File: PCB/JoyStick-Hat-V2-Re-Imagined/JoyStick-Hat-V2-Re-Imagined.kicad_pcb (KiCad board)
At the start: 4 copper layers, 123 x 56 mm, 98 parts, among them J1 20021121-00010C4LF, J11 0705430002, J2 BU2032SM-JJ-GTR, J3 0901301210, J4 0901301108, J5 RJHSE-5381, J6 1757242, J7 SBH11-PBPC-D10-ST-BK, J8 0901301108, J9 0705430002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

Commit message: V2 PCB First PAss Complete
First pass of V2 PCB Completeded !
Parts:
- added C23: C0402C104K9PACTU, AVR-KiCAD-Lib-Resistors:R0402, F.Cu at (120.5, 85.2)
- added C24: GRM155R60J475ME47D, AVR-KiCAD-Lib-Capacitors:C0402, F.Cu at (119.5, 85.2)
- added C30: C0805C103KCRACAUTO, AVR-KiCAD-Lib-Capacitors:C0805, F.Cu at (107.2, 66.8)
- added D8: SMAJ30CA, AVR-KiCAD-Lib-Diodes:SMAJ30CA, F.Cu at (101.9, 64.6)
- added J10: 0901301210, AVR-KiCAD-Lib-Connectors:CON_901301212_MOL, F.Cu at (103.8, 97.0)
- added J12: DX07S016JA1R1500, AVR-KiCAD-Lib-Connectors:JAE_DX07S016JA1R1500, F.Cu at (105.0, 74.2)
- added L4: MI0603K300R-10, AVR-KiCAD-Lib-Inductors:MI0603K300R-10, F.Cu at (109.0, 70.0)
- added R11: RC0402FR-0710KL, AVR-KiCAD-Lib-Resistors:R0402, F.Cu at (110.8, 72.2)
- added R17: RC1206FR-071ML, AVR-KiCAD-Lib-Resistors:R1206, F.Cu at (104.9, 66.6)
- added R18: RC0402FR-0722RL, AVR-KiCAD-Lib-Resistors:R0402, F.Cu at (110.7, 73.3)
- added R22: RC0402FR-0722RL, AVR-KiCAD-Lib-Resistors:R0402, F.Cu at (110.7, 74.3)
- J1, R2, R3, R4, R6, R7: moved to B.Cu
- moved R2 15.4 mm to (120.0, 99.8)
- moved R3 12.9 mm to (120.0, 98.2)
- moved J1 10.8 mm to (114.5, 96.8)
- moved R4 10.6 mm to (120.0, 96.8)
- moved R6 8.84 mm to (120.0, 95.2)
- moved R7 7.85 mm to (120.0, 93.8)
- moved D3 7.52 mm to (154.1, 99.5)
- moved D4 7.52 mm to (154.1, 98.0)
- moved R12 7.52 mm to (151.1, 99.5)
- moved R13 7.52 mm to (151.1, 98.0)
- moved J7 6.30 mm to (129.4, 105.0)
- moved D7 6.02 mm to (154.1, 107.0)
- moved R16 6.02 mm to (151.1, 107.0)
- moved D1 3.05 mm to (154.1, 102.5)
- moved D2 3.05 mm to (154.1, 101.0)
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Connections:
- R12 pad 1: unconnected-(R12-Pad1) -> /STM32F446RET6-MCU/PE2
- R13 pad 1: unconnected-(R13-Pad1) -> /STM32F446RET6-MCU/PE3
- R14 pad 1: unconnected-(R14-Pad1) -> /STM32F446RET6-MCU/PB8
- R15 pad 1: unconnected-(R15-Pad1) -> /STM32F446RET6-MCU/PB9
- R16 pad 1: unconnected-(R16-Pad1) -> /STM32F446RET6-MCU/PB7
- U1 pad 1: unconnected-(U1-PE2-Pad1) -> /STM32F446RET6-MCU/PE2
- U1 pad 2: unconnected-(U1-PE3-Pad2) -> /STM32F446RET6-MCU/PE3
- U1 pad 52: unconnected-(U1-PB13-Pad52) -> Net-(U1-PB13)
- U1 pad 53: unconnected-(U1-PB14-Pad53) -> Net-(U1-PB14)
- U1 pad 54: unconnected-(U1-PB15-Pad54) -> Net-(U1-PB15)
- U1 pad 73: unconnected-(U1-VCAP_2-Pad73) -> Net-(U1-VCAP_2)
- U1 pad 93: unconnected-(U1-PB7-Pad93) -> /STM32F446RET6-MCU/PB7
- U1 pad 95: unconnected-(U1-PB8-Pad95) -> /STM32F446RET6-MCU/PB8
- U1 pad 96: unconnected-(U1-PB9-Pad96) -> /STM32F446RET6-MCU/PB9
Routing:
- net /STM32F446RET6-MCU/SWO_TDI: track 12.2 -> 49.1 mm, vias 1 -> 0
- net /STM32F446RET6-MCU/PC10: track 0.00 -> 35.6 mm, vias 0 -> 1
- net /STM32F446RET6-MCU/SWCLK_TCK: track 11.2 -> 46.6 mm, vias 1 -> 0
- net /STM32F446RET6-MCU/NRST: track 21.2 -> 55.0 mm
- net /STM32F446RET6-MCU/SWDIO_TMS: track 8.77 -> 40.9 mm
- net Net-(U1-PD7): track 0.00 -> 32.1 mm, vias 0 -> 2
- net /STM32F446RET6-MCU/NJTRST: track 15.0 -> 46.3 mm, vias 1 -> 0
- net /STM32F446RET6-MCU/PC11: track 0.00 -> 29.5 mm, vias 0 -> 1
- net /STM32F446RET6-MCU/PC12: track 1.17 -> 29.8 mm, vias 0 -> 1
- net /STM32F446RET6-MCU/PD3: track 2.00 -> 30.5 mm, vias 0 -> 1
- net /STM32F446RET6-MCU/PB7: track 0.00 -> 27.8 mm
- net /STM32F446RET6-MCU/PD5: track 2.41 -> 29.5 mm, vias 0 -> 1
- net /STM32F446RET6-MCU/PD1: track 1.58 -> 28.2 mm, vias 0 -> 1
- net /STM32F446RET6-MCU/PB8: track 0.00 -> 25.8 mm
- net /STM32F446RET6-MCU/PD6: track 2.62 -> 28.1 mm, vias 0 -> 1
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- added copper zone on B.Cu, net Net-(C30-Pad1)
- added copper zone on F.Cu, net Net-(C30-Pad1)
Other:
- board text added: "3v3"
- board text added: "DBDI"
- board text added: "DBRQ"
- board text added: "HEARTBEAT"
- board text added: "JTAG"
- board text added: "NJRT"
- board text added: "NRST"
- board text added: "PD10"
- board text added: "PD11"
- board text added: "PD12"
- board text added: "PD13"
- board text added: "PD8"
- board text added: "STM32 EXP"
- board text added: "TCK"
- board text added: "TDI"
- board text added: "TDO"
- board text added: "TMS"
- board text added: "USB 2.0"
- board text added: "VBAT"
- board text removed: "GND / PD13"
- board text removed: "GND / PD8"
- board text removed: "PD10 / PD9"
- board text removed: "PD12 / PD11"
- board text removed: "ST HEARTBEAT"

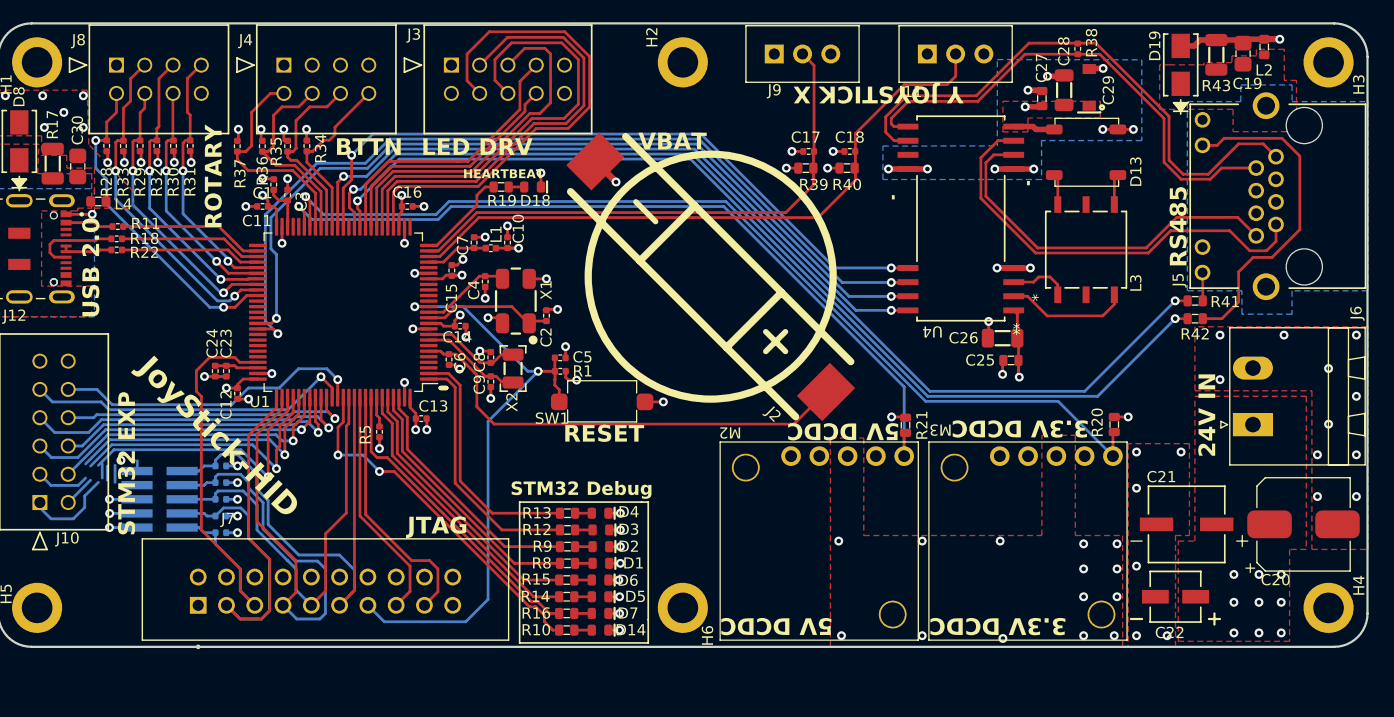
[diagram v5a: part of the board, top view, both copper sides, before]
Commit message: V2 Tweaks
More Tweaks to the completed V2 design. 3D renders of V2 design produced and added to img folder for documentation update coming in the next commit. Photos of prototype also added to img folder for documentation.
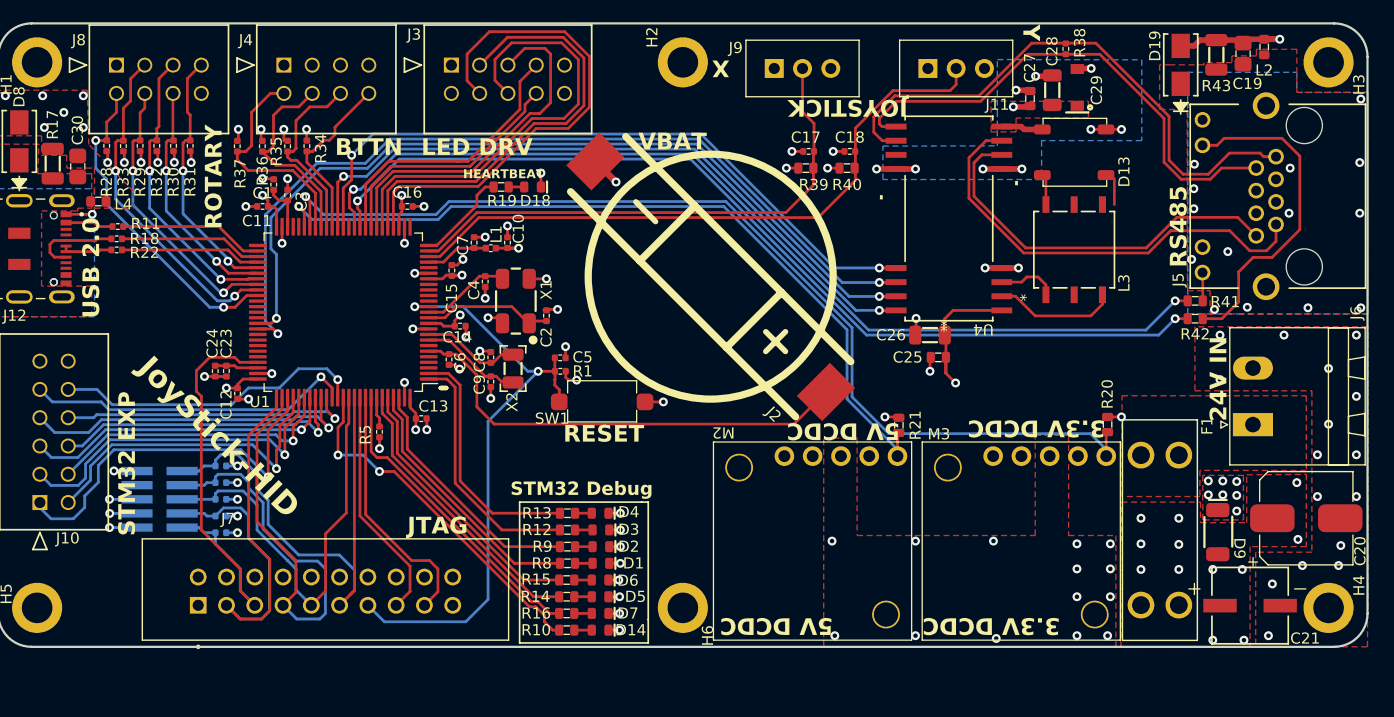
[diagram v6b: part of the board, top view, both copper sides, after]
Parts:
- removed C22: UUQ1H010MCL1GB, AVR-KiCAD-Lib-Capacitors:CAP_UUQ_4X5P4_NCH
- added D9: SMAJ24A, AVR-KiCAD-Lib-Diodes:SMAJ, F.Cu at (209.6, 99.7)
- added F1: 3557-2, AVR-KiCAD-Lib-Fuse-Holders:FUSE_3557-2, F.Cu at (204.3, 99.5)
- moved C21 9.26 mm to (212.4, 106.3), turned to 0 degrees
- moved C25 6.53 mm to (184.4, 84.0)
- moved C26 6.53 mm to (183.7, 82.0)
- moved J11 1.30 mm to (183.5, 58.0)
- moved J9 1.30 mm to (169.7, 58.0)
- moved C27 1.07 mm to (192.7, 60.8)
- moved C28 1.07 mm to (194.7, 60.0)
- moved C29 1.07 mm to (196.9, 59.8)
- moved D13 1.07 mm to (196.6, 65.6)
- moved L3 1.07 mm to (196.6, 74.3)
- moved R38 1.07 mm to (195.9, 56.3)
- moved U4 1.07 mm to (185.4, 71.5)
- moved C20 0.60 mm to (217.5, 98.5)
- moved M2 0.60 mm to (180.8, 92.9)
- moved M3 0.60 mm to (199.5, 92.9)
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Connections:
- J6 pad 1: +24V -> Net-(F1-Pad2)
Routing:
- net +3.3V: track 55.3 -> 60.7 mm
- net /RS485 To Motor Controller Interface/RS485_RX_LED: track 90.3 -> 85.7 mm
- net /RS485 To Motor Controller Interface/RS485_TX_LED: track 92.1 -> 87.6 mm
- net /Power/3.3V_PG: track 88.0 -> 91.6 mm
- net /STM32F446RET6-MCU/PC12: track 29.8 -> 31.1 mm
- net /STM32F446RET6-MCU/PC10: track 35.6 -> 34.3 mm
- net GND: track 70.8 -> 72.0 mm, vias 71 -> 77
- net /RS485 To Motor Controller Interface/Y_RS485: track 39.2 -> 40.3 mm
- net /RS485 To Motor Controller Interface/Z_RS485: track 33.8 -> 34.9 mm
- net /RS485 To Motor Controller Interface/B_RS485: track 44.6 -> 45.7 mm
- net /JoyStick Interface/JOYSTICK_X: track 49.2 -> 48.2 mm
- net /RS485 To Motor Controller Interface/RJ45_SHIELD: vias 0 -> 14
- net +24V: vias 23 -> 26
- added copper zone on F.Cu, net Net-(F1-Pad2)

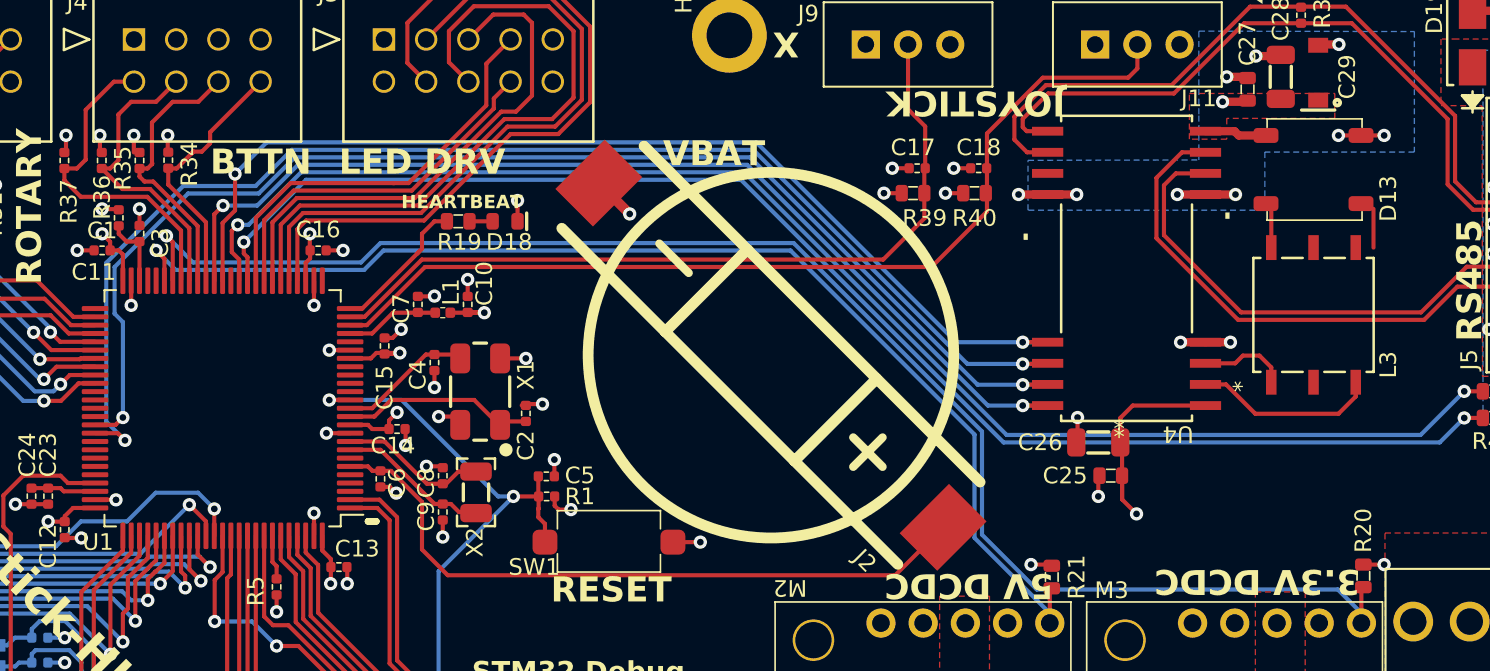
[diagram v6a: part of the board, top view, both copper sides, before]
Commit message: Schematic and board tweaks
tweaks to analog power section of MCU
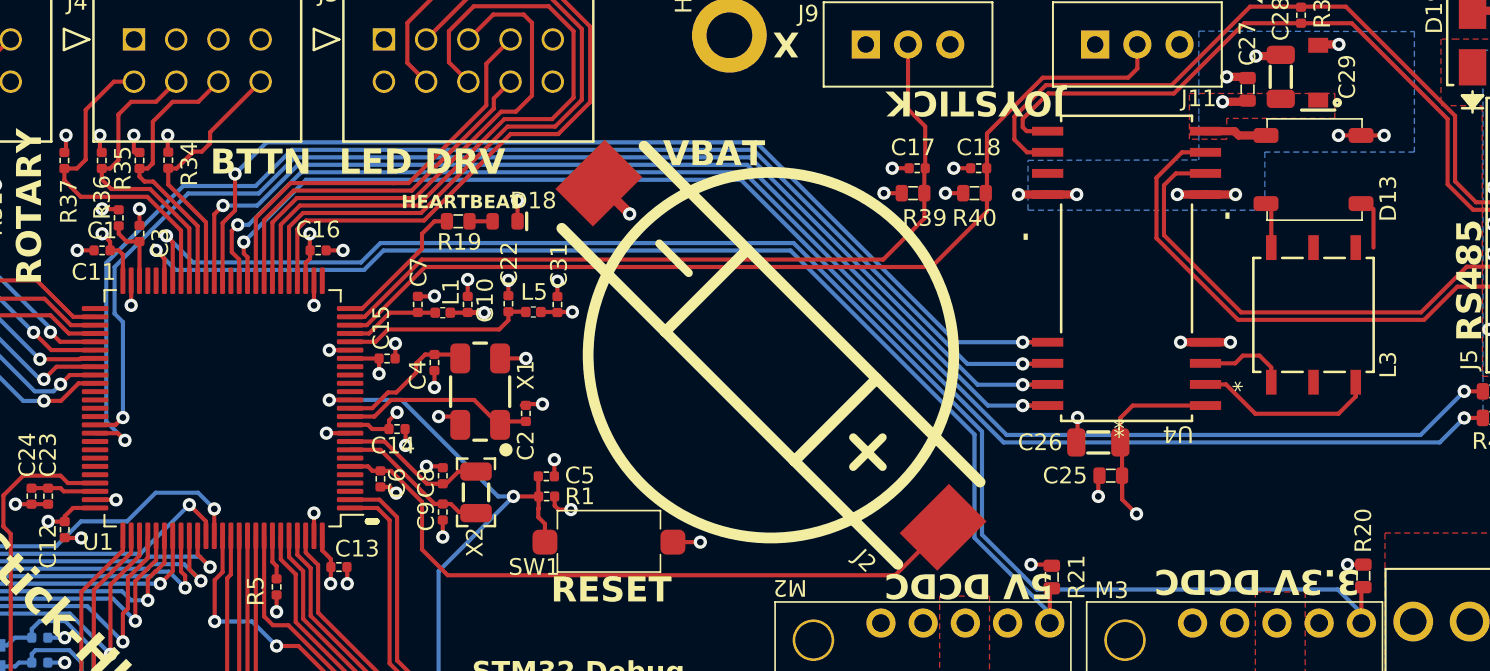
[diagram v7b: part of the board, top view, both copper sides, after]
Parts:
- added C22: C0402C104K9PACTU, AVR-KiCAD-Lib-Resistors:R0402, F.Cu at (148.2, 73.7)
- added C31: C0402C104K9PACTU, AVR-KiCAD-Lib-Resistors:R0402, F.Cu at (151.2, 73.7)
- added L5: BLM15HG601SN1D, AVR-KiCAD-Lib-Inductors:BLM15HG601SN1D, F.Cu at (149.7, 74.2)
- moved C15 0.77 mm to (140.9, 77.0), turned to 0 degrees
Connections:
- net Net-(U1-PA2) renamed /STM32F446RET6-MCU/PA2
- net Net-(U1-PD7) renamed /STM32F446RET6-MCU/PD7
- net Net-(U1-PE0) renamed /STM32F446RET6-MCU/PE0
- net Net-(U1-PE1) renamed /STM32F446RET6-MCU/PE1
- net Net-(U1-VCAP_2) renamed /STM32F446RET6-MCU/VCAP2
- U1 pad 21: unconnected-(U1-VREF+-Pad21) -> /STM32F446RET6-MCU/VREF+
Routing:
- net /STM32F446RET6-MCU/VREF+: track 0.00 -> 11.6 mm
- net GND: track 72.0 -> 73.5 mm, vias 77 -> 79
- net +3.3V: track 60.7 -> 61.1 mm, vias 29 -> 30
- added copper zone on In2.Cu, net Net-(F1-Pad2)

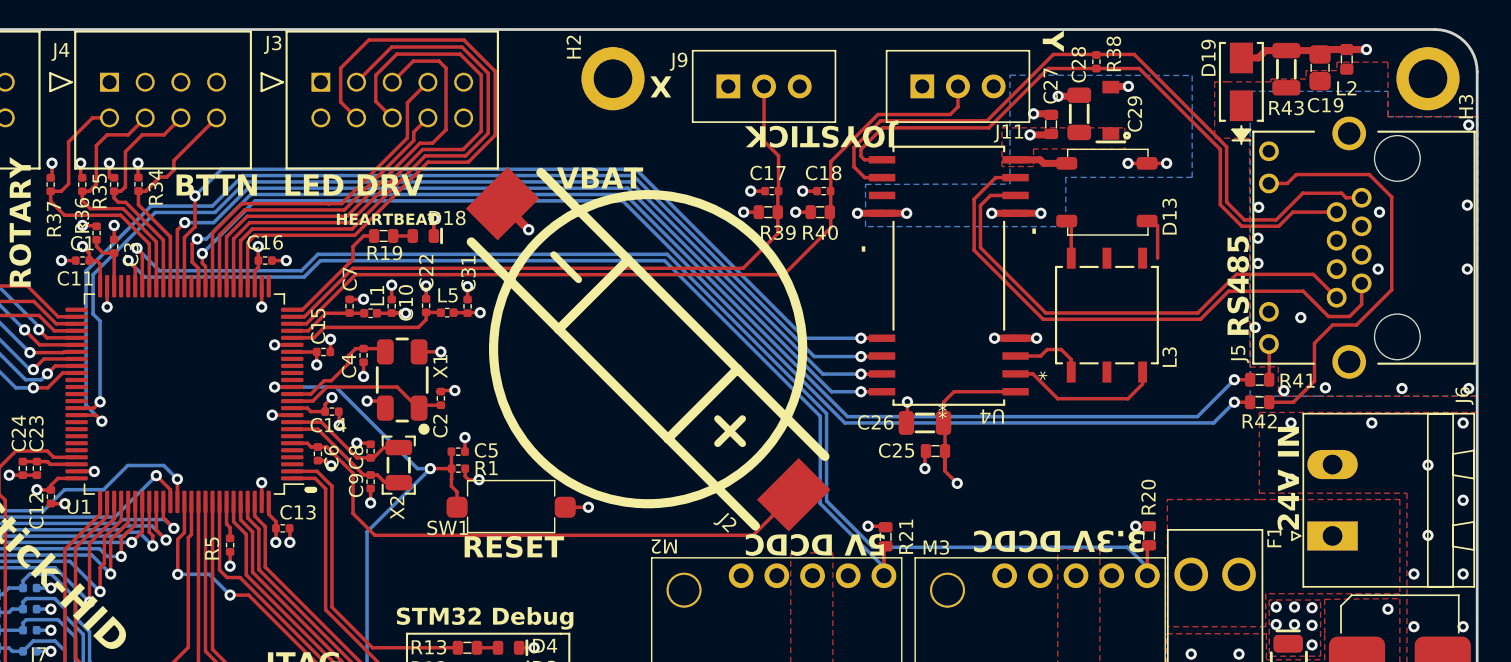
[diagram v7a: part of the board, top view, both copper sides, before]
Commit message: Daisy Chaining
Modified RS485 circuit with dual port connector for daisy chaining systems on the wheel chair !
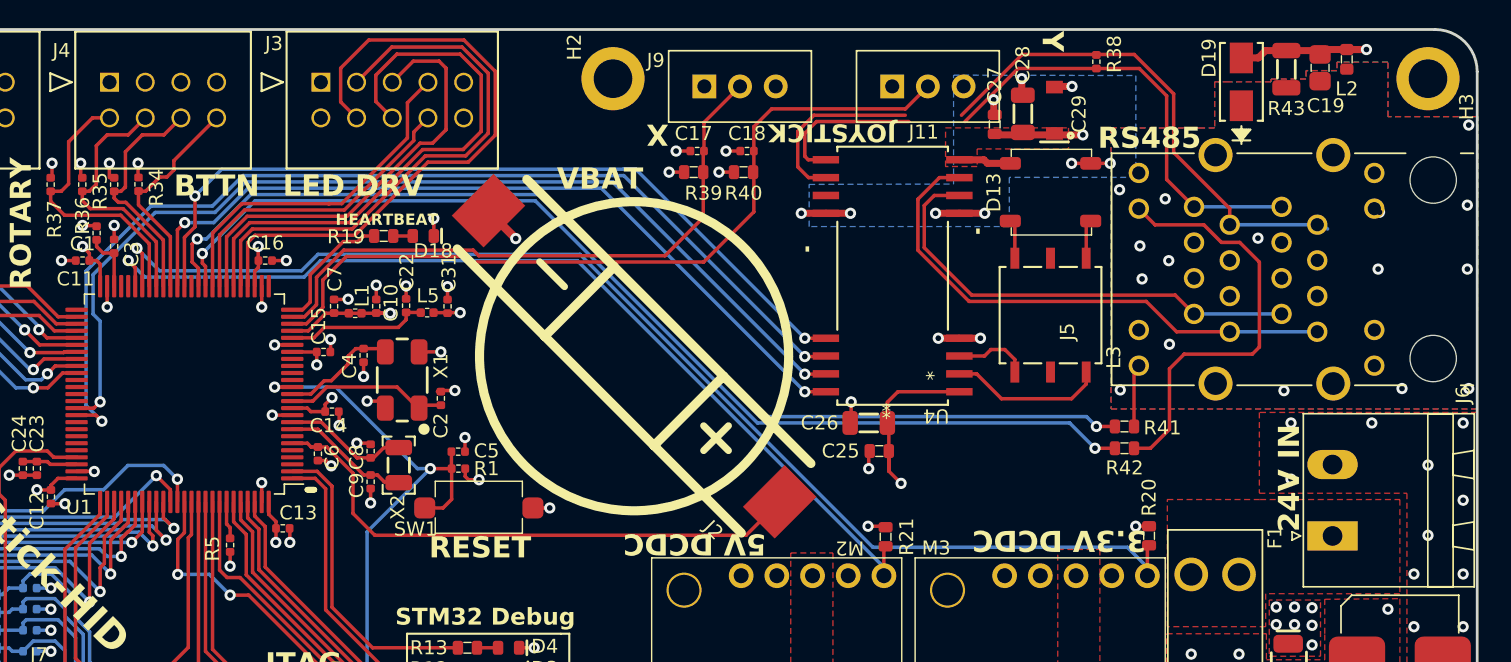
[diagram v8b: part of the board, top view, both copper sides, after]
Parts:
- J5: value RJHSE-5381 -> RJSAE-538A-02; footprint AVR-KiCAD-Lib-Connectors:AMPHENOL_RJHSE-5381 -> AVR-KiCAD-Lib-Connectors:AMPHENOL_RJSAE538A02
- moved R41 10.2 mm to (197.9, 82.2)
- moved R42 10.2 mm to (197.9, 83.8)
- moved C18 6.16 mm to (171.0, 62.6)
- moved R40 6.16 mm to (170.8, 64.2)
- moved C17 6.03 mm to (167.5, 62.6)
- moved R39 6.03 mm to (167.2, 64.2)
- moved C27 4.01 mm to (188.7, 60.8)
- moved C28 4.01 mm to (190.7, 60.0)
- moved C29 4.01 mm to (192.9, 59.8)
- moved D13 4.01 mm to (192.6, 65.6)
- moved L3 4.01 mm to (192.6, 74.3)
- moved C25 4.00 mm to (180.4, 84.0)
- moved C26 4.00 mm to (179.7, 82.0)
- moved U4 4.00 mm to (181.4, 71.5)
- moved J5 2.98 mm to (219.9, 71.1)
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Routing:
- net /RS485 To Motor Controller Interface/RS485_TX_LED: track 87.6 -> 77.2 mm
- net /RS485 To Motor Controller Interface/RS485_RX_LED: track 85.7 -> 76.2 mm
- net /RS485 To Motor Controller Interface/RS485_TX_EN: track 76.7 -> 71.7 mm
- net /RS485 To Motor Controller Interface/RS485_RX_EN: track 79.0 -> 73.9 mm
- net /RS485 To Motor Controller Interface/RS485_RXD: track 62.5 -> 57.4 mm
- net +5V: track 51.7 -> 56.6 mm
- net /RS485 To Motor Controller Interface/RS485_TXD: track 62.5 -> 58.3 mm
- net /JoyStick Interface/JOYSTICK_X: track 48.2 -> 44.1 mm
- net /Power/5V_PG: track 72.3 -> 68.6 mm
- net /Power/3.3V_PG: track 91.6 -> 88.0 mm
- net /RS485 To Motor Controller Interface/B_RS485: track 45.7 -> 42.6 mm
- net /RS485 To Motor Controller Interface/Y_RS485: track 40.3 -> 38.0 mm
- net Net-(J5-Pad12): track 2.55 -> 4.47 mm
- net /RS485 To Motor Controller Interface/Z_RS485: track 34.9 -> 33.2 mm
- net /RS485 To Motor Controller Interface/A_RS485: track 50.7 -> 49.1 mm
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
